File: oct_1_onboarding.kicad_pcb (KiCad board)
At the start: 2 copper layers, 52 parts, among them J1 REGEN_INDICATOR_33v, J10 NEU_INDICATOR_33v, J11 FOR_INDICATOR_33v, J12 REV_INDICATOR_33v, J13 CRUZ_ST_INDICATOR_33v, J14 CRUZ_EN_INDICATOR_33v, J15 EXTERNAL_RIGHTBLINK, J16 EXTERNAL_LEFTBLINK, J17 INTERNAL_RIGHTBLINK, J18 INTERNAL_LEFTBLINK, J19 EXTERNAL_HDLT, J2 CRUISE_SET, J20 EXTERNAL_BRAKELIGHT, J21 TURN_SIGNAL_SW, J22 NAME, J3 CRUISE_ENABLE, J4 Conn_01x04, J5 POS, J6 NEG, J7 LEADER, J8 TEST, J9 REGEN_INDICATOR_33v, SW1 REGEN_SW, SW2 CRUISE_SET, SW3 CRUISE_ENABLE, SW4 SPST

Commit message: completed schematic and pcb ish
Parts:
- added H1: MountingHole, MountingHole:MountingHole_3mm, F.Cu at (162.2, 110.9)
- added H2: MountingHole, MountingHole:MountingHole_3mm, F.Cu at (76.2, 110.5)
- added H3: MountingHole, MountingHole:MountingHole_3mm, F.Cu at (162.2, 28.3)
- added H4: MountingHole, MountingHole:MountingHole_3mm, F.Cu at (77.5, 27.9)
- added LOGO1: Dr. Hallock Logo, UTSVT_Special:Hallock_Image_Tiny, F.Cu at (139.7, 85.1)
- added LOGO2: UTSVT Logo, UTSVT_Special:UTSVT_Logo_Symbol, F.Cu at (124.5, 86.4)
- J1: value REGEN_INDICATOR_33v -> REGEN_IND_33v; footprint Connector_Molex:Molex_Micro-Fit_3.0_43045-1000_2x05_P3.00mm_Horizontal -> Connector_Molex:Molex_Micro-Fit_3.0_43650-0200_1x02_P3.00mm_Horizontal
- J10: value NEU_INDICATOR_33v -> NEU_IND_33v; footprint Connector_Molex:Molex_Micro-Fit_3.0_43650-0210_1x02-1MP_P3.00mm_Horizontal -> Connector_Molex:Molex_Micro-Fit_3.0_43650-0200_1x02_P3.00mm_Horizontal
- J11: value FOR_INDICATOR_33v -> FOR_IND_33v; footprint Connector_Molex:Molex_Micro-Fit_3.0_43650-0210_1x02-1MP_P3.00mm_Horizontal -> Connector_Molex:Molex_Micro-Fit_3.0_43650-0200_1x02_P3.00mm_Horizontal
- J12: value REV_INDICATOR_33v -> REV_IND_33v; footprint Connector_Molex:Molex_Micro-Fit_3.0_43650-0210_1x02-1MP_P3.00mm_Horizontal -> Connector_Molex:Molex_Micro-Fit_3.0_43650-0200_1x02_P3.00mm_Horizontal
- J13: value CRUZ_ST_INDICATOR_33v -> CRUZ_ST; footprint Connector_Molex:Molex_Micro-Fit_3.0_43650-0210_1x02-1MP_P3.00mm_Horizontal -> Connector_Molex:Molex_Micro-Fit_3.0_43650-0200_1x02_P3.00mm_Horizontal
- J14: value CRUZ_EN_INDICATOR_33v -> CRUZ_EN; footprint Connector_Molex:Molex_Micro-Fit_3.0_43650-0210_1x02-1MP_P3.00mm_Horizontal -> Connector_Molex:Molex_Micro-Fit_3.0_43650-0200_1x02_P3.00mm_Horizontal
- J15: value EXTERNAL_RIGHTBLINK -> EXT_RBLINK; footprint Connector_Molex:Molex_Micro-Fit_3.0_43650-0210_1x02-1MP_P3.00mm_Horizontal -> Connector_Molex:Molex_Micro-Fit_3.0_43650-0200_1x02_P3.00mm_Horizontal
- J16: value EXTERNAL_LEFTBLINK -> EXT_LBLINK; footprint Connector_Molex:Molex_Micro-Fit_3.0_43650-0210_1x02-1MP_P3.00mm_Horizontal -> Connector_Molex:Molex_Micro-Fit_3.0_43650-0200_1x02_P3.00mm_Horizontal
- J17: value INTERNAL_RIGHTBLINK -> INT_RBLINK; footprint Connector_Molex:Molex_Micro-Fit_3.0_43650-0210_1x02-1MP_P3.00mm_Horizontal -> Connector_Molex:Molex_Micro-Fit_3.0_43650-0200_1x02_P3.00mm_Horizontal
- J18: value INTERNAL_LEFTBLINK -> INT_LBLINK; footprint Connector_Molex:Molex_Micro-Fit_3.0_43650-0210_1x02-1MP_P3.00mm_Horizontal -> Connector_Molex:Molex_Micro-Fit_3.0_43650-0200_1x02_P3.00mm_Horizontal
- J19: value EXTERNAL_HDLT -> EXT_HDLT; footprint Connector_Molex:Molex_Micro-Fit_3.0_43650-0210_1x02-1MP_P3.00mm_Horizontal -> Connector_Molex:Molex_Micro-Fit_3.0_43650-0200_1x02_P3.00mm_Horizontal
- J2, J22, J3, J7, J8: footprint Connector_Molex:Molex_Micro-Fit_3.0_43650-0210_1x02-1MP_P3.00mm_Horizontal -> Connector_Molex:Molex_Micro-Fit_3.0_43650-0200_1x02_P3.00mm_Horizontal
- J20: value EXTERNAL_BRAKELIGHT -> EXT_BLIGHT; footprint Connector_Molex:Molex_Micro-Fit_3.0_43650-0210_1x02-1MP_P3.00mm_Horizontal -> Connector_Molex:Molex_Micro-Fit_3.0_43650-0200_1x02_P3.00mm_Horizontal
- J9: value REGEN_INDICATOR_33v -> REGEN_IND_33v; footprint Connector_Molex:Molex_Micro-Fit_3.0_43650-0210_1x02-1MP_P3.00mm_Horizontal -> Connector_Molex:Molex_Micro-Fit_3.0_43650-0200_1x02_P3.00mm_Horizontal
- R1, R10, R11, R12, R2, R3, R4, R5, R7, R8, R9: moved to B.Cu
- SW1: footprint Connector_Molex:Molex_Micro-Fit_3.0_43650-0400_1x04_P3.00mm_Horizontal -> UTSVT_Special:2MS6T1B3M2QES
- moved J8 173.9 mm to (81.3, 63.7), turned to 90 degrees
- moved J7 171.8 mm to (81.3, 75.8), turned to 90 degrees
- moved J22 171.8 mm to (88.7, 33.2)
- moved J18 170.8 mm to (145.8, 34.5)
- moved J6 162.9 mm to (133.3, 31.8), turned to 90 degrees
- moved D10 159.7 mm to (146.4, 40.6), turned to 0 degrees
- moved R10 157.0 mm to (141.0, 38.5), turned to 90 degrees
- moved SW4 154.0 mm to (99.1, 41.1), turned to 180 degrees
- moved J15 123.7 mm to (157.0, 75.1), turned to -90 degrees
- moved J5 121.0 mm to (118.1, 31.8), turned to 90 degrees
- moved R7 111.4 mm to (162.2, 80.9), turned to 90 degrees
- moved SW2 106.2 mm to (90.2, 41.1), turned to 180 degrees
- moved D7 103.3 mm to (148.6, 81.3)
- moved J21 92.9 mm to (157.0, 57.5), turned to -90 degrees
- moved J2 85.6 mm to (81.4, 40.9), turned to 90 degrees
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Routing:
- net Net-(J6-Pad1): track 0.00 -> 93.9 mm
- net Net-(J5-Pad1): track 0.00 -> 82.5 mm
- net Net-(D12-Pad2): track 0.00 -> 30.1 mm, vias 0 -> 1
- net Net-(J4-Pad2): track 0.00 -> 26.8 mm
- net Net-(D1-Pad2): track 0.00 -> 22.7 mm, vias 0 -> 1
- net Net-(D8-Pad2): track 0.00 -> 21.0 mm, vias 0 -> 1
- net Net-(D3-Pad2): track 0.00 -> 20.2 mm, vias 0 -> 1
- net Net-(J21-Pad2): track 0.00 -> 19.5 mm
- net Net-(D2-Pad2): track 0.00 -> 19.0 mm, vias 0 -> 1
- net Net-(J21-Pad1): track 0.00 -> 17.7 mm
- net Net-(J4-Pad1): track 0.00 -> 17.5 mm
- net Net-(J22-Pad1): track 0.00 -> 17.3 mm
- net Net-(J21-Pad3): track 0.00 -> 17.2 mm
- net Net-(D6-Pad2): track 0.00 -> 17.0 mm, vias 0 -> 1
- net Net-(J4-Pad3): track 0.00 -> 17.0 mm
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- added copper zone on B.Cu, net Net-(J6-Pad1)
- added copper zone on F.Cu, net Net-(J6-Pad1)
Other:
- board outline added: 99.1 x 96.5 mm

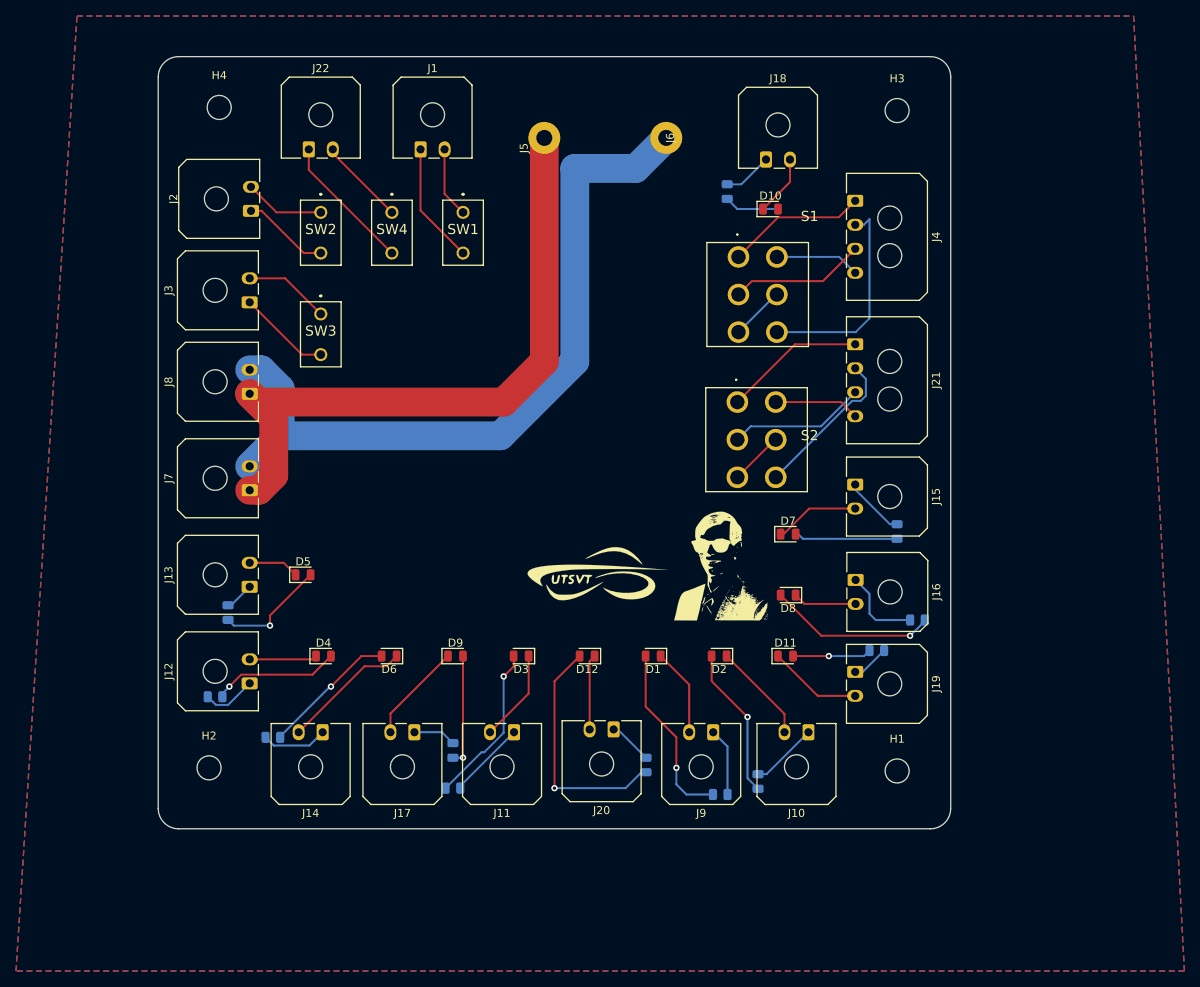
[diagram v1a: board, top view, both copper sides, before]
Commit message: added datasheets
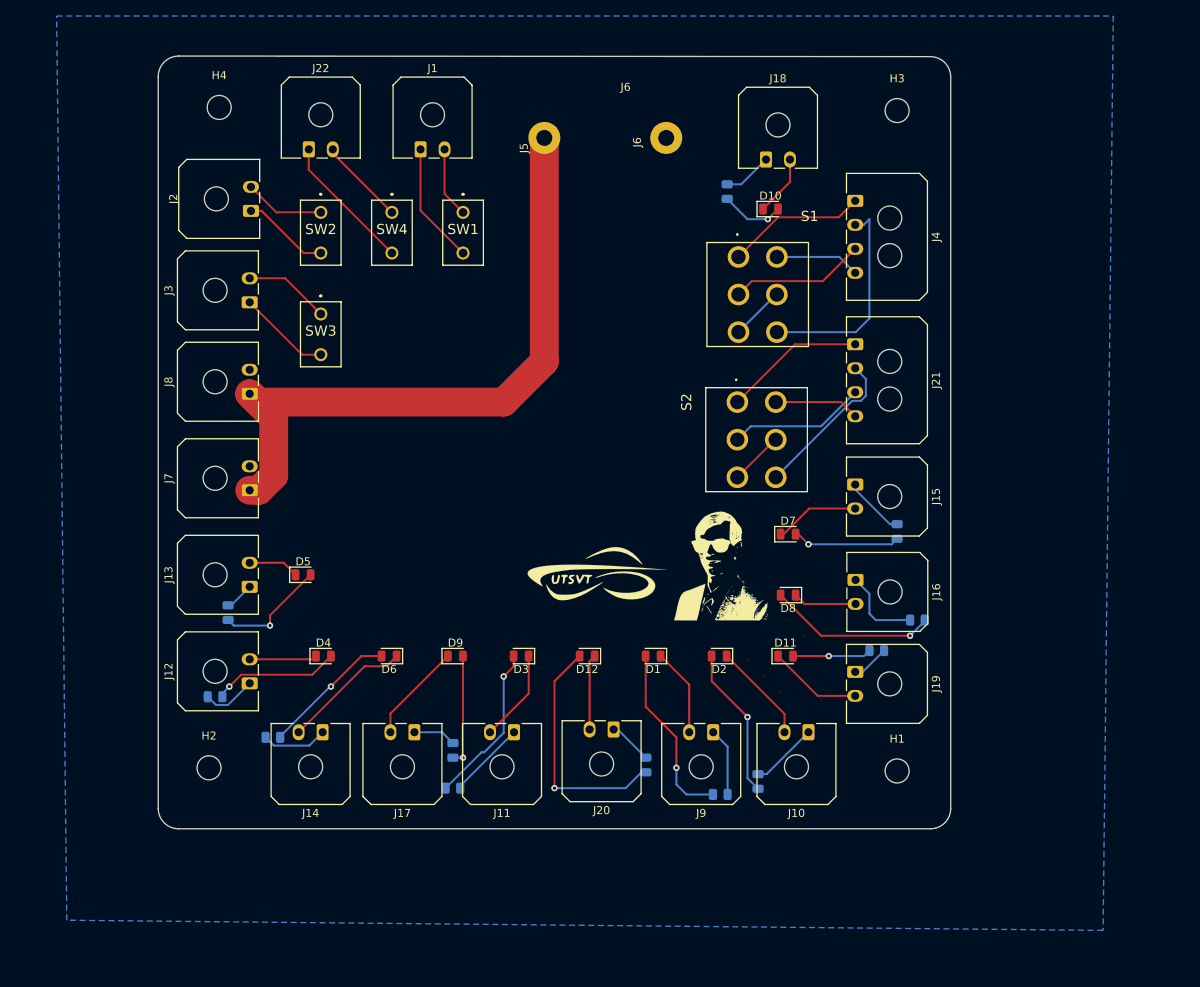
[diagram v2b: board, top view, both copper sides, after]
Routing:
- net Net-(J6-Pad1): track 93.9 -> 0.00 mm
- net Net-(D10-Pad2): track 6.88 -> 7.93 mm, vias 0 -> 1
- net Net-(D7-Pad2): track 12.6 -> 13.5 mm, vias 0 -> 1
- removed copper zone on F.Cu, net Net-(J6-Pad1)
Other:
- board size 99.1 x 96.5 mm -> 99.1 x 96.6 mm
- board text added: "J6"
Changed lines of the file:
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@@
     (property "Sheetname" "")
     (attr through_hole)
-    (fp_text reference "S2" (at 9.03 4.175) (layer "F.SilkS")
+    (fp_text reference "S2" (at -6.35 0 90) (layer "F.SilkS")
       (effects (font (size 1.27 1.27) (thickness 0.254)))
     )
@@
     (property "Sheetname" "")
     (attr through_hole)
-    (fp_text reference "J6" (at 0 0.5 90) (layer "F.SilkS")
+    (fp_text reference "J6" (at -0.55 -3.615 90) (layer "F.SilkS")
       (effects (font (size 1 1) (thickness 0.15)))
     )
@@
     (property "Sheetname" "")
     (attr smd)
-    (fp_text reference "R4" (at 0 1.65) (layer "B.SilkS")
+    (fp_text reference "R4" (at 2.0225 1.65) (layer "B.SilkS")
       (effects (font (size 1 1) (thickness 0.15)) (justify mirror))
     )
@@
   )
   (gr_arc (start 72.39 118.11) (mid 70.593949 117.366051) (end 69.85 115.57) (layer "Edge.Cuts") (width 0.1))
+  (gr_line (start 166.37 21.59) (end 72.436671 21.514549) (layer "Edge.Cuts") (width 0.1))
   (gr_line (start 72.39 118.11) (end 166.37 118.11) (layer "Edge.Cuts") (width 0.1))
-  (gr_circle (center 72.39 21.59) (end 72.39 21.59) (layer "Edge.Cuts") (width 0.1) (fill none))
   (gr_line (start 168.91 115.57) (end 168.91 24.13) (layer "Edge.Cuts") (width 0.1))
   (gr_line (start 69.85 24.13) (end 69.85 115.57) (layer "Edge.Cuts") (width 0.1))
   (gr_arc (start 168.91 115.57) (mid 168.166051 117.366051) (end 166.37 118.11) (layer "Edge.Cuts") (width 0.1))
-  (gr_arc (start 69.85 24.13) (mid 70.593949 22.333949) (end 72.39 21.59) (layer "Edge.Cuts") (width 0.1))
   (gr_arc (start 166.37 21.59) (mid 168.166051 22.333949) (end 168.91 24.13) (layer "Edge.Cuts") (width 0.1))
-  (gr_line (start 166.37 21.59) (end 72.39 21.59) (layer "Edge.Cuts") (width 0.1))
-  (dimension (type aligned) (layer "Edge.Cuts")
-    (pts (xy 69.85 121.92) (xy 168.91 121.92))
-    (height 0)
-    (gr_text "99.0600 mm" (at 119.38 120.77) (layer "Edge.Cuts")
-      (effects (font (size 1 1) (thickness 0.15)))
-    )
-    (format (units 3) (units_format 1) (precision 4))
-    (style (thickness 0.1) (arrow_length 1.27) (text_position_mode 0) (extension_height 0.58642) (extension_offset 0.5) keep_text_aligned)
-  )
-  (dimension (type aligned) (layer "Edge.Cuts")
-    (pts (xy 176.53 21.59) (xy 176.53 118.11))
-    (height -1.27)
-    (gr_text "96.5200 mm" (at 176.65 69.85 90) (layer "Edge.Cuts")
-      (effects (font (size 1 1) (thickness 0.15)))
-    )
-    (format (units 3) (units_format 1) (precision 4))
-    (style (thickness 0.1) (arrow_length 1.27) (text_position_mode 0) (extension_height 0.58642) (extension_offset 0.5) keep_text_aligned)
+  (gr_arc (start 69.850001 24.13) (mid 70.5894 22.274434) (end 72.436671 21.514549) (layer "Edge.Cuts") (width 0.1))
+  (gr_text "J6" (at 128.27 25.4) (layer "F.SilkS")
+    (effects (font (size 1 1) (thickness 0.15)))
   )
   (segment (start 136.219 100.08543) (end 136.219 106.04) (width 0.25) (layer "F.Cu") (net 1))
@@
   (segment (start 151.225666 78.0775) (end 148.023166 81.28) (width 0.25) (layer "F.Cu") (net 13))
   (segment (start 156.97 78.0775) (end 151.225666 78.0775) (width 0.25) (layer "F.Cu") (net 13))
-  (segment (start 150.4375 81.8575) (end 149.86 81.28) (width 0.25) (layer "B.Cu") (net 14))
-  (segment (start 162.21 81.8575) (end 150.4375 81.8575) (width 0.25) (layer "B.Cu") (net 14))
+  (segment (start 149.5275 81.28) (end 149.86 81.28) (width 0.25) (layer "F.Cu") (net 14))
+  (segment (start 149.86 81.28) (end 151.13 82.55) (width 0.25) (layer "F.Cu") (net 14))
+  (via (at 151.13 82.55) (size 0.8) (drill 0.4) (layers "F.Cu" "B.Cu") (net 14))
+  (segment (start 162.21 81.8575) (end 161.5175 82.55) (width 0.25) (layer "B.Cu") (net 14))
+  (segment (start 161.5175 82.55) (end 151.13 82.55) (width 0.25) (layer "B.Cu") (net 14))
   (segment (start 149.5275 88.9) (end 150.63 90.0025) (width 0.25) (layer "F.Cu") (net 15))
   (segment (start 150.63 90.0025) (end 157.015 90.0025) (width 0.25) (layer "F.Cu") (net 15))
@@
   (segment (start 145.445 40.64) (end 148.82 37.265) (width 0.25) (layer "F.Cu") (net 19))
   (segment (start 148.82 37.265) (end 148.82 34.45) (width 0.25) (layer "F.Cu") (net 19))
-  (segment (start 142.24 40.64) (end 147.32 40.64) (width 0.25) (layer "B.Cu") (net 20))
-  (segment (start 140.97 39.37) (end 142.24 40.64) (width 0.25) (layer "B.Cu") (net 20))
+  (segment (start 147.32 40.64) (end 146.05 41.91) (width 0.25) (layer "F.Cu") (net 20))
+  (via (at 146.05 41.91) (size 0.8) (drill 0.4) (layers "F.Cu" "B.Cu") (net 20))
+  (segment (start 146.05 41.91) (end 143.51 41.91) (width 0.25) (layer "B.Cu") (net 20))
+  (segment (start 143.51 41.91) (end 140.97 39.37) (width 0.25) (layer "B.Cu") (net 20))
   (segment (start 147.32 96.52) (end 152.295 101.495) (width 0.25) (layer "F.Cu") (net 21))
   (segment (start 152.295 101.495) (end 156.97 101.495) (width 0.25) (layer "F.Cu") (net 21))
@@
   (segment (start 118.11 31.75) (end 118.11 59.69) (width 3.6) (layer "F.Cu") (net 51))
   (segment (start 113.03 64.77) (end 82.32 64.77) (width 3.6) (layer "F.Cu") (net 51))
-  (segment (start 121.92 35.56) (end 121.92 59.69) (width 3.6) (layer "B.Cu") (net 52))
-  (segment (start 112.625 68.985) (end 85.09 68.985) (width 3.6) (layer "B.Cu") (net 52))
-  (segment (start 81.28 60.73) (end 82.72198 60.73) (width 3.6) (layer "B.Cu") (net 52))
-  (segment (start 82.72198 60.73) (end 85.09 63.09802) (width 3.6) (layer "B.Cu") (net 52))
-  (segment (start 129.54 35.56) (end 121.92 35.56) (width 3.6) (layer "B.Cu") (net 52))
-  (segment (start 121.92 59.69) (end 112.625 68.985) (width 3.6) (layer "B.Cu") (net 52))
-  (segment (start 85.09 68.985) (end 81.28 72.795) (width 3.6) (layer "B.Cu") (net 52))
-  (segment (start 85.09 63.09802) (end 85.09 68.985) (width 3.6) (layer "B.Cu") (net 52))
-  (segment (start 133.35 31.75) (end 129.54 35.56) (width 3.6) (layer "B.Cu") (net 52))
   (segment (start 142.38 56.025) (end 147.08 51.325) (width 0.25) (layer "B.Cu") (net 53))
   (segment (start 147.08 51.325) (end 147.18 51.325) (width 0.25) (layer "B.Cu") (net 53))
@@
   (segment (start 99.06 41.0575) (end 91.67 33.6675) (width 0.25) (layer "F.Cu") (net 56))
   (segment (start 91.67 33.6675) (end 91.67 33.18) (width 0.25) (layer "F.Cu") (net 56))
-  (zone (net 52) (net_name "Net-(J6-Pad1)") (layers F&B.Cu) (hatch edge 0.508)
-    (connect_pads (clearance 0.508))
+  (zone (net 52) (net_name "Net-(J6-Pad1)") (layer "B.Cu") (hatch edge 0.508)
+    (connect_pads yes (clearance 0.508))
     (min_thickness 0.254) (filled_areas_thickness no)
     (fill yes (thermal_gap 0.508) (thermal_bridge_width 0.508))
     (polygon
       (pts
-        (xy 198.12 135.89)
-        (xy 52.07 135.89)
-        (xy 59.69 16.51)
-        (xy 191.77 16.51)
+        (xy 187.96 130.81)
+        (xy 58.42 129.54)
+        (xy 57.15 16.51)
+        (xy 189.23 16.51)
       )
     )
